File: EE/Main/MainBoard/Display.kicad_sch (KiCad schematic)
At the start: 0 parts

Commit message: Updated layout, and placement for main board
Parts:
- added Q1, Q2, Q3, Q4: 2N7002NXAKR, Package_TO_SOT_SMD:SC-59, symbol Device:Q_NMOS_GSD
- added R10, R11, R12, R13, R7, R8, R9: 560, Resistor_SMD:R_0402_1005Metric, symbol Device:R
- added R3, R4, R5, R6: 10k, Resistor_SMD:R_0402_1005Metric, symbol Device:R
- added U2: DA04-11EWA, Display_7Segment:DA04-11SURKWA, symbol Display_Character:DA04-11EWA
- added U3: DA04-11GWA, Display_7Segment:DA04-11CGKWA, symbol Display_Character:DA04-11GWA
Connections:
- new net A: R7.2, U2.10 (DIG2_A), U2.15 (DIG1_A), U3.10 (DIG2_A), U3.15 (DIG1_A)
- new net A_EN: R7.1
- new net B: R8.2, U2.12 (DIG2_B), U2.13 (DIG1_B), U3.12 (DIG2_B), U3.13 (DIG1_B)
- new net B_EN: R8.1
- new net C: R9.2, U2.1 (DIG1_C), U2.8 (DIG2_C), U3.1 (DIG1_C), U3.8 (DIG2_C)
- new net C_EN: R9.1
- new net D: R10.2, U2.3 (DIG1_D), U2.6 (DIG2_D), U3.3 (DIG1_D), U3.6 (DIG2_D)
- new net D1_G: Q2.2 (S), U3.4 (DIG1_CA)
- new net D1_G_EN: Q2.1 (G), R4.1
- new net D1_R: Q1.2 (S), U2.4 (DIG1_CA)
- new net D1_R_EN: Q1.1 (G), R3.1
- new net D2_G: Q4.2 (S), U3.5 (DIG2_CA)
- new net D2_G_EN: Q4.1 (G), R6.1
- new net D2_R: Q3.2 (S), U2.5 (DIG2_CA)
- new net D2_R_EN: Q3.1 (G), R5.1
- new net D_EN: R10.1
- new net E: R11.2, U2.2 (DIG1_E), U2.7 (DIG2_E), U3.2 (DIG1_E), U3.7 (DIG2_E)
- new net E_EN: R11.1
- new net F: R12.2, U2.11 (DIG2_F), U2.14 (DIG1_F), U3.11 (DIG2_F), U3.14 (DIG1_F)
- new net F_EN: R12.1
- new net G: R13.2, U2.16 (DIG1_G), U2.9 (DIG2_G), U3.16 (DIG1_G), U3.9 (DIG2_G)
- new net GND: Q1.3 (D), Q2.3 (D), Q3.3 (D), Q4.3 (D), R3.2, R4.2, R5.2, R6.2
- new net G_EN: R13.1

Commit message: Routine Update
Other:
- note added: "TODO no longer the EWA - likely LDD-A406NI"
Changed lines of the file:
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@@
 (kicad_sch (version 20211123) (generator eeschema)
   (paper "A4")
+  (text "TODO no longer the EWA - likely  LDD-A406NI" (at 61.468 64.516 0)
+    (effects (font (size 1.27 1.27)) (justify left bottom))
+  )
   (label "D" (at 102.108 85.09 0)
     (effects (font (size 1.27 1.27)) (justify left bottom))

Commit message: Random Check in
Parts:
- removed Q1, Q2, Q3, Q4: 2N7002NXAKR, Package_TO_SOT_SMD:SC-59, symbol Device:Q_NMOS_GSD
- removed R10, R11, R12, R13, R7, R8, R9: 560, Resistor_SMD:R_0402_1005Metric, symbol Device:R
- removed R3, R4, R5, R6: 10k, Resistor_SMD:R_0402_1005Metric, symbol Device:R
- removed U2: DA04-11EWA, Display_7Segment:DA04-11SURKWA, symbol Display_Character:DA04-11EWA
- removed U3: DA04-11GWA, Display_7Segment:DA04-11CGKWA, symbol Display_Character:DA04-11GWA
- added J9: Conn_01x04_Male, symbol Connector:Conn_01x04_Male
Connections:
- net GND: now also J9.4 (Pin_4)
- new net DISPLAY_DIN: J9.2 (Pin_2)
- new net Vdrive: J9.1 (Pin_1)
- no-connect marks 0 -> 1
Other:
- note added: "TODO RGB LED Footprint"
- note removed: "TODO no longer the EWA - likely LDD-A406NI"

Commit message: First pass layout
Assumes using Cut-through RGB 7 Segment
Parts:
- J9: footprint (none) -> Library:RGB_7Segment
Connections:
- net DISPLAY_DIN: now also J9.3 (Pin_3); no longer J9.2 (Pin_2)
- net GND: now also J9.1 (Pin_1); no longer J9.4 (Pin_4)
- net Vdrive: now also J9.2 (Pin_2); no longer J9.1 (Pin_1)
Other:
- moved on the sheet: J9
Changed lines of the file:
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@@
 	(paper "A4")
 	(no_connect
-		(at 160.274 102.87)
+		(at 142.24 109.22)
 	)
 	(text "TODO RGB LED Footprint\n"
 		(exclude_from_sim no)
-		(at 148.082 88.646 0)
+		(at 130.048 92.456 0)
+		(effects
+			(font
+				(size 1.27 1.27)
+			)
+			(justify left bottom)
+		)
+	)
+	(label "DISPLAY_DIN"
+		(at 142.24 106.68 0)
+		(fields_autoplaced yes)
 		(effects
 			(font
@@
 	)
 	(label "V_DISPLAY"
+		(at 142.24 104.14 0)
+		(fields_autoplaced yes)
+		(effects
+			(font
+				(size 1.27 1.27)
+			)
+			(justify left bottom)
+		)
+	)
+	(label "V_DISPLAY"
 		(at 21.59 36.83 270)
 		(fields_autoplaced yes)
@@
 			)
 			(justify right bottom)
-		)
-	)
-	(label "V_DISPLAY"
-		(at 160.274 97.79 0)
-		(fields_autoplaced yes)
-		(effects
-			(font
-				(size 1.27 1.27)
-			)
-			(justify left bottom)
-		)
-	)
-	(label "DISPLAY_DIN"
-		(at 160.274 100.33 0)
-		(fields_autoplaced yes)
-		(effects
-			(font
-				(size 1.27 1.27)
-			)
-			(justify left bottom)
 		)
 	)
@@
 	(symbol
 		(lib_id "power:GND")
-		(at 160.274 105.41 0)
+		(at 142.24 101.6 180)
 		(unit 1)
 		(exclude_from_sim no)
@@
 		(dnp no)
 		(fields_autoplaced yes)
-		(property "Reference" "#PWR0125"
-			(at 160.274 111.76 0)
+		(property "Reference" "#PWR028"
+			(at 142.24 95.25 0)
 			(effects
 				(font
@@
 		)
 		(property "Value" "GND"
-			(at 160.274 109.8534 0)
+			(at 142.24 97.4669 0)
 			(effects
 				(font
@@
 		)
 		(property "Footprint" ""
-			(at 160.274 105.41 0)
+			(at 142.24 101.6 0)
 			(effects
 				(font
@@
 		)
 		(property "Datasheet" ""
-			(at 160.274 105.41 0)
+			(at 142.24 101.6 0)
 			(effects
 				(font
@@
 		)
 		(property "Description" ""
-			(at 160.274 105.41 0)
+			(at 142.24 101.6 0)
 			(effects
 				(font
@@
 		)
 		(instances
-			(project ""
+			(project "MainBoard"
 				(path "/dfe0084c-a900-4f47-8966-915ebf3a8e75/8b04ffa1-873f-4cda-b1fe-4981fdbc7b42"
-					(reference "#PWR0125")
+					(reference "#PWR028")
 					(unit 1)
 				)
@@
 	(symbol
 		(lib_id "Connector:Conn_01x04_Male")
-		(at 155.194 100.33 0)
+		(at 137.16 104.14 0)
 		(unit 1)
 		(exclude_from_sim no)
@@
 		(dnp no)
 		(property "Reference" "J9"
-			(at 155.829 94.014 0)
+			(at 137.795 97.824 0)
 			(effects
 				(font
@@
 		)
 		(property "Value" "Conn_01x04_Male"
-			(at 152.146 100.33 90)
-			(effects
-				(font
-					(size 1.27 1.27)
-				)
-			)
-		)
-		(property "Footprint" ""
-			(at 155.194 100.33 0)
+			(at 134.112 104.14 90)
+			(effects
+				(font
+					(size 1.27 1.27)
+				)
+			)
+		)
+		(property "Footprint" "Library:RGB_7Segment"
+			(at 137.16 104.14 0)
 			(effects
 				(font
@@
 		)
 		(property "Datasheet" "~"
-			(at 155.194 100.33 0)
+			(at 137.16 104.14 0)
 			(effects
 				(font
@@
 		)
 		(property "Description" ""
-			(at 155.194 100.33 0)
-			(effects
-				(font
+			(at 137.16 104.14 0)
+			(effects
+				(font

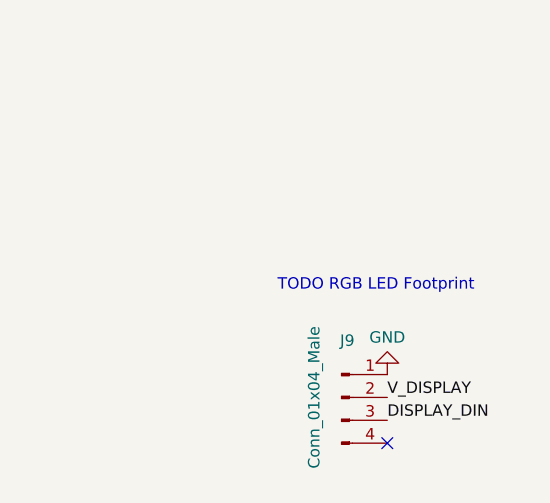
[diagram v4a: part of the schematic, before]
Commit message: Potential Layout. Need to confirm button and L&F.
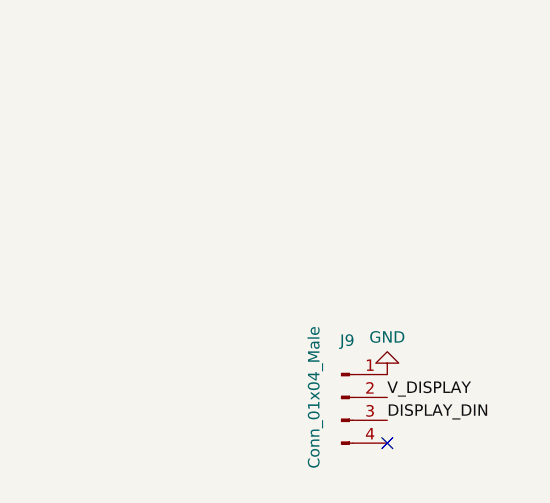
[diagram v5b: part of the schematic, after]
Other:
- note removed: "TODO RGB LED Footprint"
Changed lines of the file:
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@@
 		(at 142.24 109.22)
-	)
-	(text "TODO RGB LED Footprint\n"
-		(exclude_from_sim no)
-		(at 130.048 92.456 0)
-		(effects
-			(font
-				(size 1.27 1.27)
-			)
-			(justify left bottom)
-		)
 	)
 	(label "DISPLAY_DIN"

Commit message: Potential Revision
Potentially fabb-able rev.
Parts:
- removed J9: Conn_01x04_Male, Library:RGB_7Segment, symbol Connector:Conn_01x04_Male
- added J9: Conn_01x06, Library:RGB_7Segment, symbol Connector_Generic:Conn_01x06
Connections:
- net DISPLAY_DIN: now also J9.6 (Pin_6)
- net GND: now also J9.1 (Pin_1)
- new net +3V3: J9.2 (Pin_2)
- new net DISPLAY_CIN: J9.5 (Pin_5)
- no-connect marks 1 -> 2
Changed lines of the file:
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@@
 	(paper "A4")
 	(no_connect
-		(at 142.24 109.22)
-	)
-	(label "DISPLAY_DIN"
-		(at 142.24 106.68 0)
-		(fields_autoplaced yes)
-		(effects
-			(font
-				(size 1.27 1.27)
-			)
-			(justify left bottom)
-		)
+		(at 138.43 125.73)
+	)
+	(no_connect
+		(at 138.43 128.27)
 	)
 	(label "DISPLAY_DIN"
@@
 		)
 	)
+	(label "DISPLAY_CIN"
+		(at 138.43 123.19 0)
+		(fields_autoplaced yes)
+		(effects
+			(font
+				(size 1.27 1.27)
+			)
+			(justify left bottom)
+		)
+	)
+	(label "DISPLAY_DIN"
+		(at 138.43 120.65 0)
+		(fields_autoplaced yes)
+		(effects
+			(font
+				(size 1.27 1.27)
+			)
+			(justify left bottom)
+		)
+	)
+	(label "DISPLAY_CIN"
+		(at 25.4 26.67 0)
+		(fields_autoplaced yes)
+		(effects
+			(font
+				(size 1.27 1.27)
+			)
+			(justify left bottom)
+		)
+	)
 	(label "V_DISPLAY"
-		(at 142.24 104.14 0)
+		(at 138.43 130.81 0)
 		(fields_autoplaced yes)
 		(effects
@@
 		)
 	)
+	(hierarchical_label "DISPLAY_CIN"
+		(shape input)
+		(at 25.4 26.67 180)
+		(fields_autoplaced yes)
+		(effects
+			(font
+				(size 1.27 1.27)
+			)
+			(justify right)
+		)
+	)
 	(symbol
-		(lib_id "power:Vdrive")
+		(lib_id "Connector_Generic:Conn_01x06")
+		(at 133.35 128.27 180)
+		(unit 1)
+		(exclude_from_sim no)
+		(in_bom yes)
+		(on_board yes)
+		(dnp no)
+		(fields_autoplaced yes)
+		(property "Reference" "J9"
+			(at 133.35 115.2355 0)
+			(effects
+				(font
+					(size 1.27 1.27)
+				)
+			)
+		)
+		(property "Value" "Conn_01x06"
+			(at 133.35 117.6598 0)
+			(effects
+				(font
+					(size 1.27 1.27)
+				)
+			)
+		)
+		(property "Footprint" "Library:RGB_7Segment"
+			(at 133.35 128.27 0)
+			(effects
+				(font
+					(size 1.27 1.27)
+				)
+				(hide yes)
+			)
+		)
+		(property "Datasheet" "~"
+			(at 133.35 128.27 0)
+			(effects
+				(font
+					(size 1.27 1.27)
+				)
+				(hide yes)
+			)
+		)
+		(property "Description" "Generic connector, single row, 01x06, script generated (kicad-library-utils/schlib/autogen/connector/)"
+			(at 133.35 128.27 0)
+			(effects
+				(font
+					(size 1.27 1.27)
+				)
+				(hide yes)
+			)
+		)
+		(pin "5"
+		)
+		(pin "1"
+		)
+		(pin "3"
+		)
+		(pin "2"
+		)
+		(pin "6"
+		)
+		(pin "4"
+		)
+		(instances
+			(project ""
+				(path "/dfe0084c-a900-4f47-8966-915ebf3a8e75/8b04ffa1-873f-4cda-b1fe-4981fdbc7b42"
+					(reference "J9")
+					(unit 1)
+				)
+			)
+		)
+	)
+	(symbol
+		(lib_id "power:+3V3")
 		(at 21.59 36.83 0)
 		(unit 1)
@@
 		(dnp no)
 		(fields_autoplaced yes)
-		(property "Reference" "#PWR05"
+		(property "Reference" "#PWR02"
 			(at 21.59 40.64 0)
 			(effects
@@
 			)
 		)
-		(property "Value" "Vdrive"
+		(property "Value" "+3V3"
 			(at 21.59 32.6969 0)
 			(effects
@@
 			)
 		)
-		(property "Description" "Power symbol creates a global label with name \"Vdrive\""
+		(property "Description" "Power symbol creates a global label with name \"+3V3\""
 			(at 21.59 36.83 0)
 			(effects
@@
 		)
 		(instances
-			(project "MainBoard"
+			(project ""
 				(path "/dfe0084c-a900-4f47-8966-915ebf3a8e75/8b04ffa1-873f-4cda-b1fe-4981fdbc7b42"
-					(reference "#PWR05")
+					(reference "#PWR02")
 					(unit 1)
 				)
@@
 	(symbol
 		(lib_id "power:GND")
-		(at 142.24 101.6 180)
+		(at 138.43 133.35 0)
 		(unit 1)
 		(exclude_from_sim no)
@@
 		(fields_autoplaced yes)
 		(property "Reference" "#PWR028"
-			(at 142.24 95.25 0)
+			(at 138.43 139.7 0)
 			(effects
 				(font
@@
 		)
 		(property "Value" "GND"
-			(at 142.24 97.4669 0)
+			(at 138.43 137.4831 0)
 			(effects
 				(font
@@
 		)
 		(property "Footprint" ""
-			(at 142.24 101.6 0)
+			(at 138.43 133.35 0)
 			(effects
 				(font
@@
 		)
 		(property "Datasheet" ""
-			(at 142.24 101.6 0)
+			(at 138.43 133.35 0)
 			(effects
 				(font
@@
 		)
 		(property "Description" ""
-			(at 142.24 101.6 0)
+			(at 138.43 133.35 0)
 			(effects
 				(font
@@
 					(unit 1)
 				)
-			)
-		)
-	)
-	(symbol
-		(lib_id "Connector:Conn_01x04_Male")
-		(at 137.16 104.14 0)
-		(unit 1)
-		(exclude_from_sim no)
-		(in_bom yes)
-		(on_board yes)
-		(dnp no)
-		(property "Reference" "J9"
-			(at 137.795 97.824 0)
-			(effects
-				(font
-					(size 1.27 1.27)
-				)
-			)
-		)
-		(property "Value" "Conn_01x04_Male"
-			(at 134.112 104.14 90)
-			(effects
-				(font
-					(size 1.27 1.27)
-				)
-			)
-		)
-		(property "Footprint" "Library:RGB_7Segment"
-			(at 137.16 104.14 0)
-			(effects
-				(font
-					(size 1.27 1.27)
-				)
-				(hide yes)
-			)
-		)
-		(property "Datasheet" "~"
-			(at 137.16 104.14 0)
-			(effects
-				(font
-					(size 1.27 1.27)
-				)
-				(hide yes)
-			)
-		)
-		(property "Description" ""
-			(at 137.16 104.14 0)
-			(effects
-				(font
-					(size 1.27 1.27)
-				)
-				(hide yes)
-			)
-		)
-		(pin "1"
-		)
-		(pin "2"
-		)
-		(pin "3"
-		)
-		(pin "4"
-		)
-		(instances
-			(project ""
-				(path "/dfe0084c-a900-4f47-8966-915ebf3a8e75/8b04ffa1-873f-4cda-b1fe-4981fdbc7b42"
-					(reference "J9")
-					(unit 1)
-				)
